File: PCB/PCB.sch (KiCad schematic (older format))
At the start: 10 parts

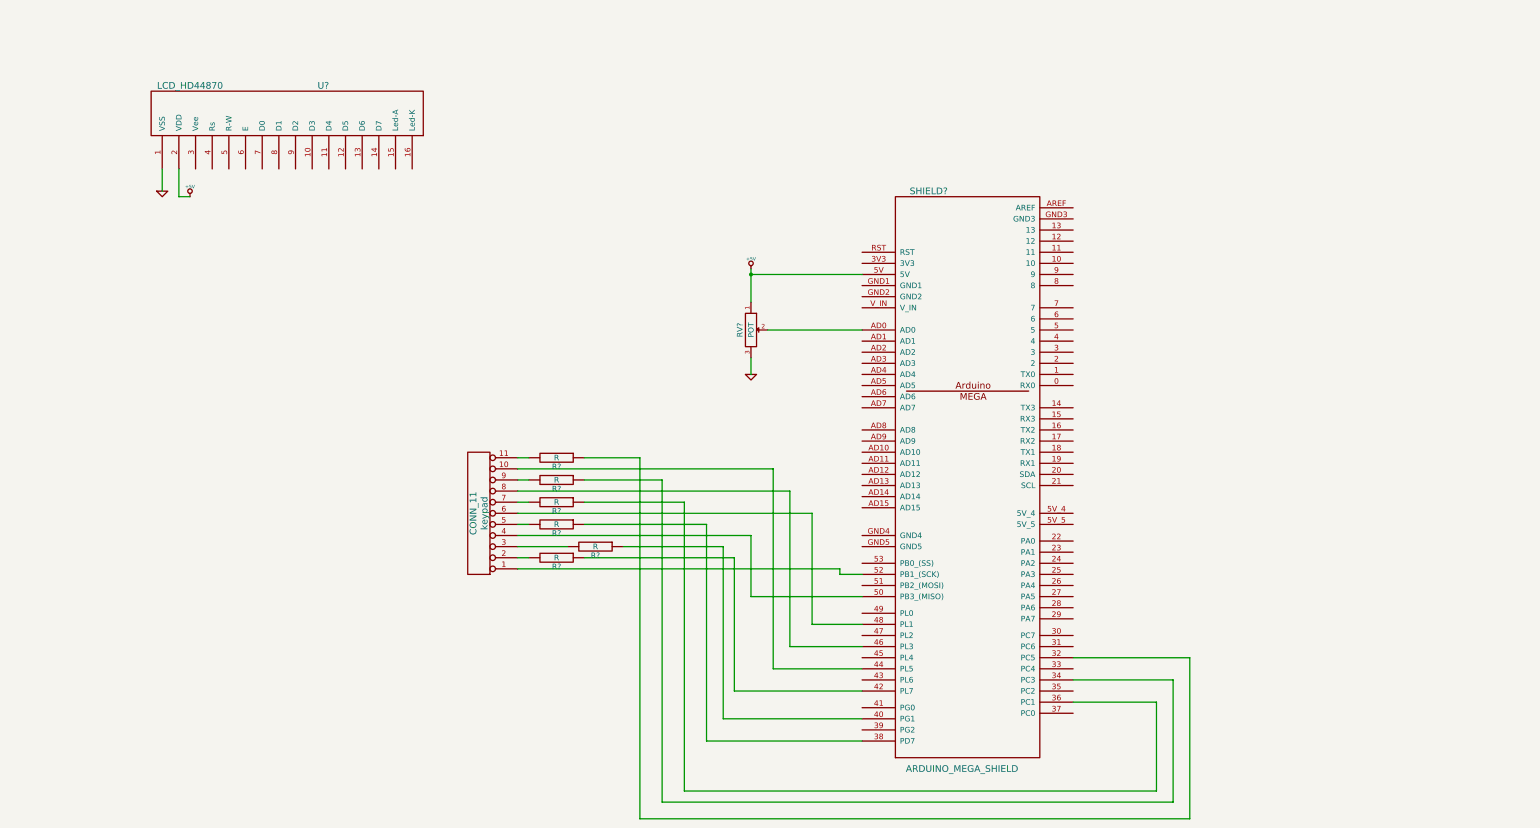
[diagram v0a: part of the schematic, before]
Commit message: Creo componente DS1820 y diseño control backligth
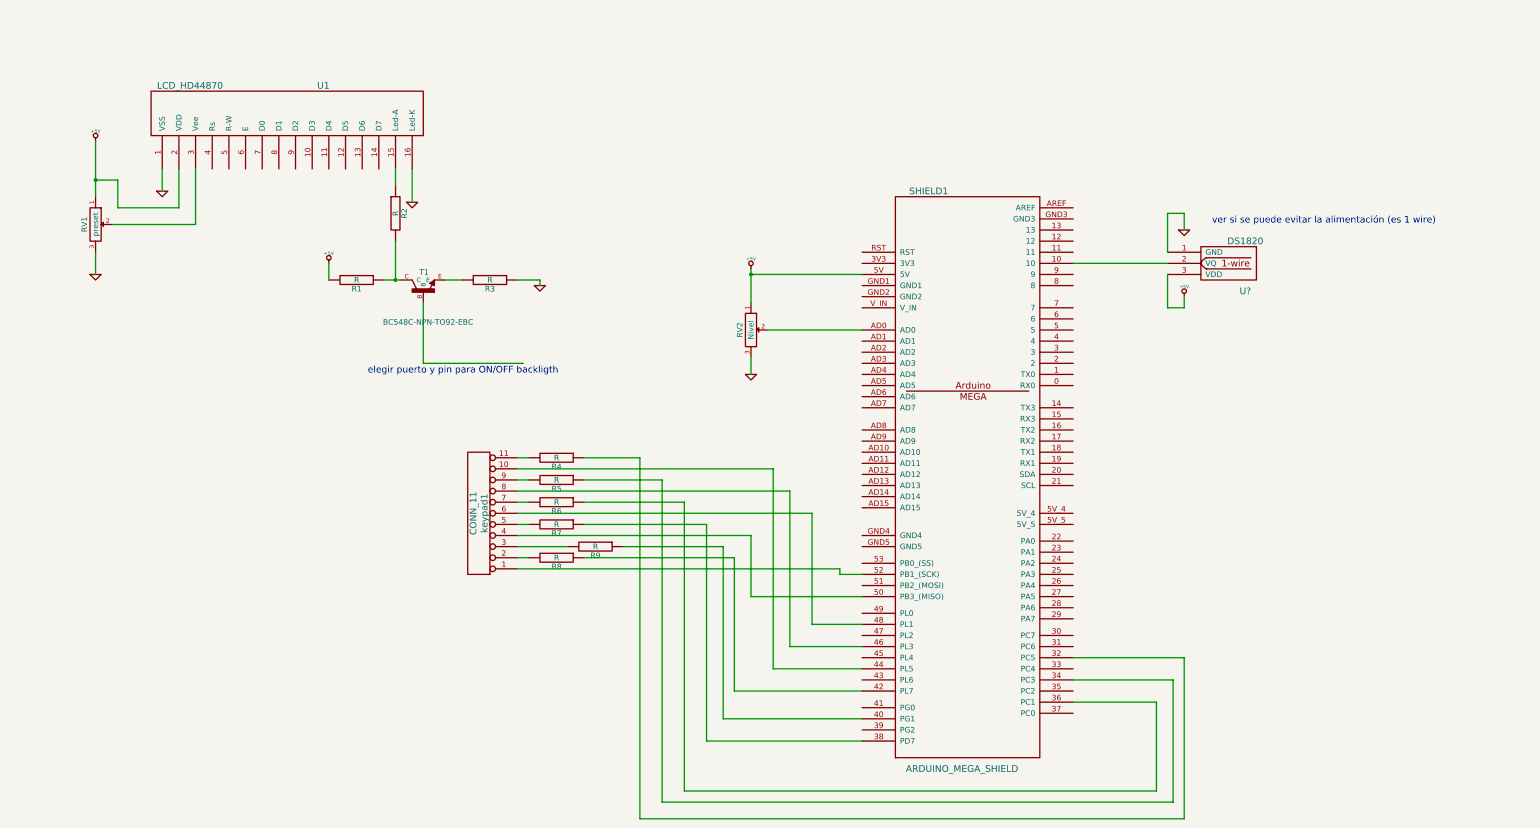
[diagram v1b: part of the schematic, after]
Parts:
- added R1, R2, R3: R, symbol R
- added RV1: preset, symbol POT
- added T1: BC548C-NPN-TO92-EBC, transistor-TO92-EBC, symbol BC548C-NPN-TO92-EBC
- added U?: DS1820, symbol DS1820
- RV2: renamed from RV?; value POT -> Nivel
- gave numbers to parts that had none: 8
- renumbered keypad to keypad1
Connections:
- net +5V: now also R1.2, RV1.1, U?.3 (VDD)
- net GND: now also U1.16 (Led-K), R3.1, RV1.3, U?.1 (GND)
- net at SHIELD1.10: now also U?.2 (VQ)
- net at U1.15 (Led-A): now also R2.1
- net at U1.3 (Vee): now also RV1.2
- new net: R1.1, R2.2, T1.C
- new net: R3.2, T1.E
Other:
- note added: "elegir puerto y pin para ON/OFF backligth"
- note added: "ver si se puede evitar la alimentación (es 1 wire)"

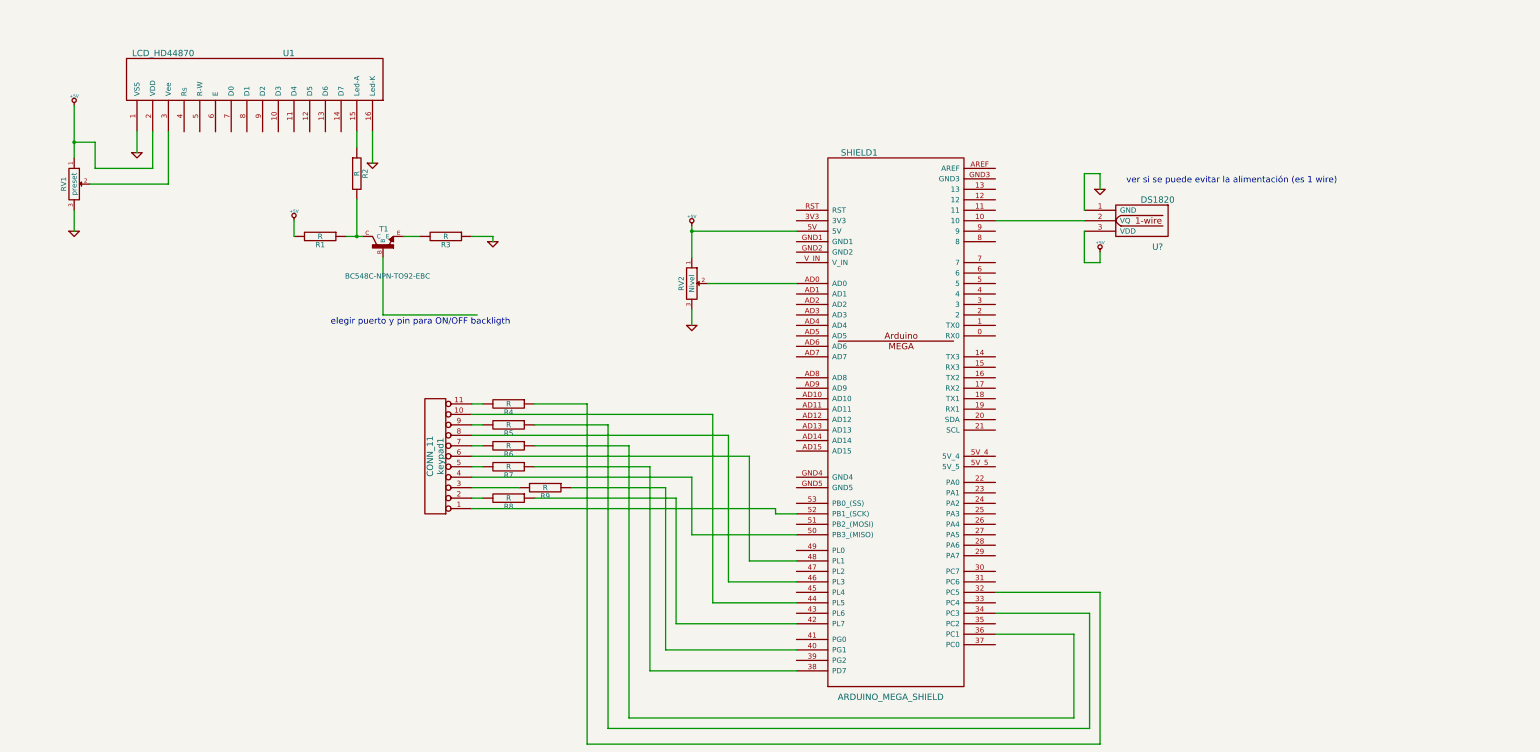
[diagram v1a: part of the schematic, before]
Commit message: Esquemático del PCB actualizado. Se mejoraron y completaron funciones: seteo alertas y menu.
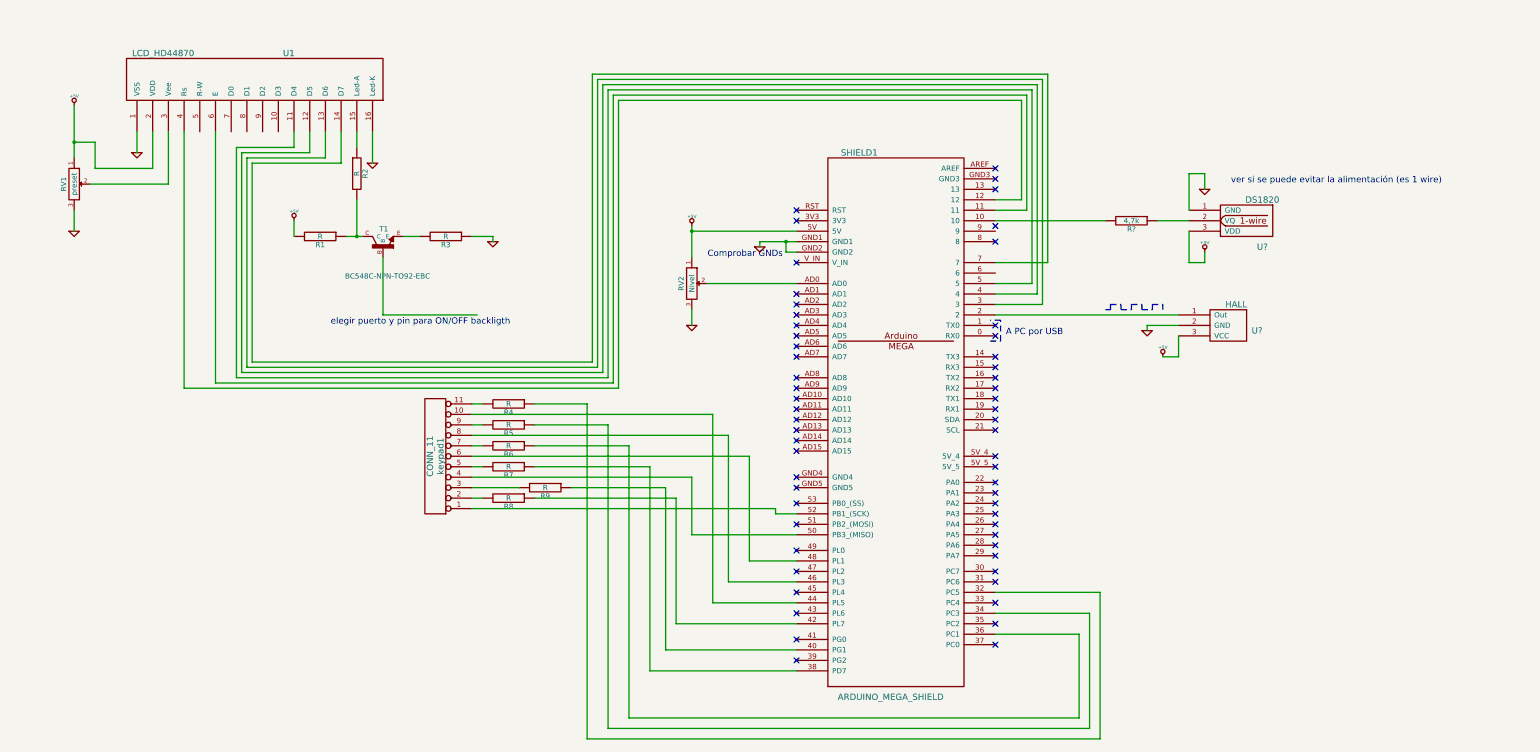
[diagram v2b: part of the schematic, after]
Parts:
- added R?: 4,7k, symbol R
- added U?: HALL, symbol HALL
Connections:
- net +5V: now also U?.3 (VCC)
- net GND: now also SHIELD1.GND1, SHIELD1.GND2, U?.2 (GND)
- net at SHIELD1.10: now also R?.2; no longer U?.2 (VQ)
- net at SHIELD1.11: now also U1.6 (E)
- net at SHIELD1.12: now also U1.4 (Rs)
- net at SHIELD1.2: now also U?.1 (Out)
- net at SHIELD1.3: now also U1.13 (D6)
- net at SHIELD1.4: now also U1.12 (D5)
- net at SHIELD1.5: now also U1.11 (D4)
- net at SHIELD1.7: now also U1.14 (D7)
- new net: R?.1, U?.2 (VQ)
- no-connect marks 0 -> 58
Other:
- note added: "A PC por USB"
- note added: "Comprobar GNDs\n\n"
- moved on the sheet: U?

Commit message: PCB iniciado
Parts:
- added P1: back +5V, symbol CONN_2
- gave numbers to parts that had none: 3
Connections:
- net +5V: now also SHIELD1.5V_4, SHIELD1.5V_5, P1.2 (PM)
- net GND: now also SHIELD1.GND3, SHIELD1.GND4, SHIELD1.GND5
- net at SHIELD1.39 (PG2): now also T1.B
- net at R1.1, R2.2, T1.C: now also P1.1 (P1)
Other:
- note added: "Comprobar esos 5 pines que no se conectan"
- note added: "Elijo ON/OFF backligth transistor o +5V\nSi puenteo directo no sueldo R1 ni T1"
- note removed: "Comprobar GNDs\n\n"
- note removed: "elegir puerto y pin para ON/OFF backligth"
- moved on the sheet: R1, R3, T1
